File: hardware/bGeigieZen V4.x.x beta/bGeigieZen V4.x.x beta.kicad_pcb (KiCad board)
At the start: 2 copper layers, 129.4 x 64.6 mm, 12 parts, among them J1 M5 2x15 pin, J2 Geiger IRover, J3 GPS, J4 Geiger Safepulse, J5 Extra support header, J6 Grove

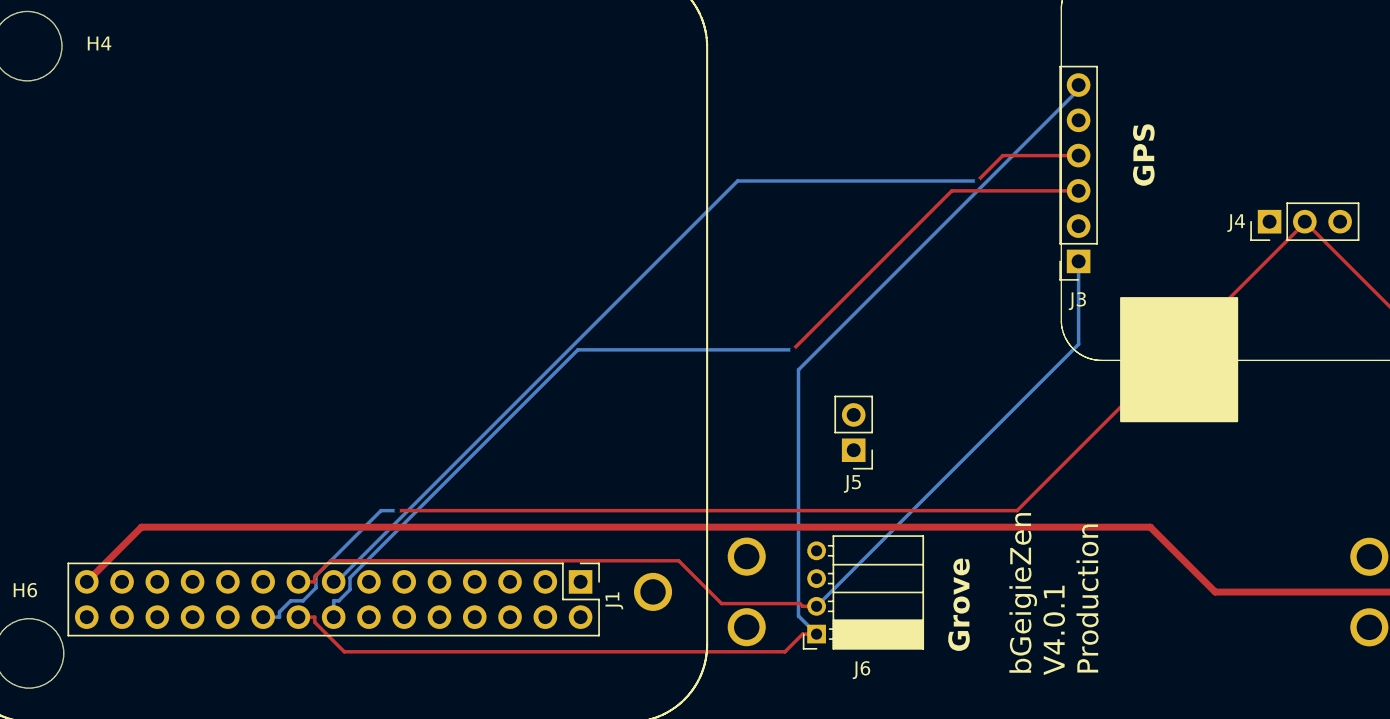
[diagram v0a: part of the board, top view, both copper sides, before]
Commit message: Small changes in copyright year and screen saver text
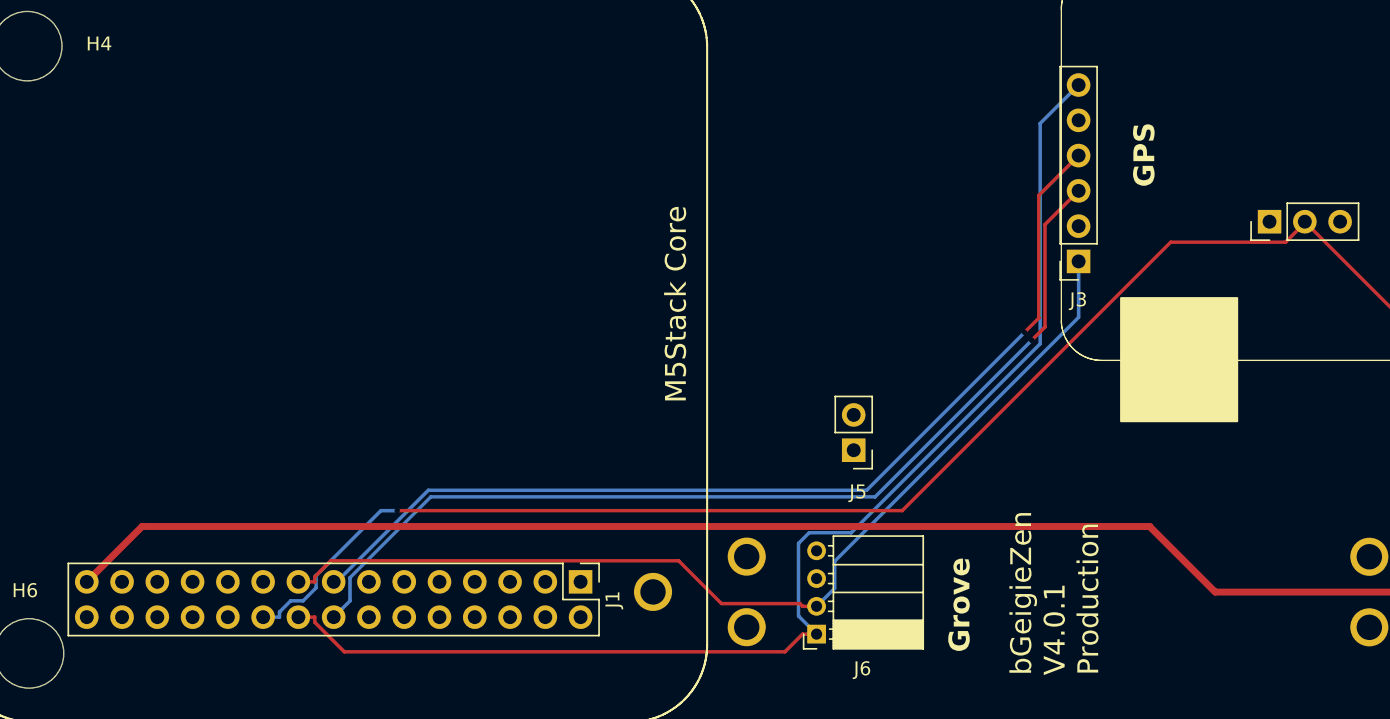
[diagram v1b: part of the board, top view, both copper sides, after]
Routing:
- net /RX2: track 66.4 -> 71.5 mm
- net /TX2: track 67.5 -> 71.7 mm
- net /SCL: track 87.5 -> 89.3 mm
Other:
- board text added: "M5Stack Core"
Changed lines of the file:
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@@
 (kicad_pcb
-	(version 20240108)
+	(version 20240225)
 	(generator "pcbnew")
 	(generator_version "8.99")
@@
 		(tags "Through hole pin header THT 1x02 2.54mm single row")
 		(property "Reference" "J5"
-			(at 0 -2.33 0)
+			(at -0.3208 -3.005 0)
 			(unlocked yes)
 			(layer "F.SilkS")
@@
 		(tags "Through hole pin header THT 1x03 2.54mm single row")
 		(property "Reference" "J4"
-			(at 0 -2.33 0)
+			(at 0.098 -3.4632 0)
 			(unlocked yes)
-			(layer "F.SilkS")
+			(layer "B.SilkS")
 			(effects
 				(font
@@
 					(thickness 0.15)
 				)
+				(justify mirror)
 			)
 		)
@@
 		)
 	)
+	(gr_text "M5Stack Core"
+		(at 148.336 96.4172 90)
+		(layer "F.SilkS")
+		(effects
+			(font
+				(size 1.5 1.5)
+				(thickness 0.3)
+			)
+		)
+	)
 	(gr_text "screws for the display are M3 12mm"
 		(at 106.7816 141.426 0)
@@
 	)
 	(segment
-		(start 177.317 85.7097)
-		(end 171.863 85.7097)
+		(start 174.4472 97.4154)
+		(end 174.4472 88.5795)
 		(width 0.25)
 		(layer "F.Cu")
@@
 	)
 	(segment
-		(start 171.863 85.7097)
-		(end 170.0347 87.538)
+		(start 173.4223 98.4403)
+		(end 174.4472 97.4154)
+		(width 0.25)
+		(layer "F.Cu")
+		(net 2)
+	)
+	(segment
+		(start 174.4472 88.5795)
+		(end 177.317 85.7097)
 		(width 0.25)
 		(layer "F.Cu")
@@
 	)
 	(via
-		(at 170.0347 87.538)
+		(at 173.4223 98.4403)
 		(size 0.3)
 		(drill 0.4)
@@
 	)
 	(segment
-		(start 123.8941 116.407)
-		(end 123.6726 116.407)
+		(start 162.052 109.8106)
+		(end 130.4905 109.8106)
 		(width 0.25)
 		(layer "B.Cu")
@@
 	)
 	(segment
-		(start 170.0347 87.538)
-		(end 152.7631 87.538)
+		(start 173.4223 98.4403)
+		(end 162.052 109.8106)
 		(width 0.25)
 		(layer "B.Cu")
@@
 	)
 	(segment
-		(start 152.7631 87.538)
+		(start 123.8941 116.407)
+		(end 123.6726 116.407)
+		(width 0.25)
+		(layer "B.Cu")
+		(net 2)
+	)
+	(segment
+		(start 130.4905 109.8106)
 		(end 123.8941 116.407)
 		(width 0.25)
@@
 	)
 	(segment
-		(start 177.317 88.2497)
-		(end 168.1844 88.2497)
+		(start 174.8972 98.05)
+		(end 174.8972 90.6695)
 		(width 0.25)
 		(layer "F.Cu")
@@
 	)
 	(segment
-		(start 168.1844 88.2497)
-		(end 156.739 99.6951)
+		(start 173.9392 99.008)
+		(end 174.8972 98.05)
+		(width 0.25)
+		(layer "F.Cu")
+		(net 3)
+	)
+	(segment
+		(start 174.8972 90.6695)
+		(end 177.317 88.2497)
 		(width 0.25)
 		(layer "F.Cu")
@@
 	)
 	(via
-		(at 156.739 99.6951)
+		(at 173.9392 99.008)
 		(size 0.3)
 		(drill 0.4)
@@
 	)
 	(segment
-		(start 123.6726 118.947)
-		(end 123.6726 117.7703)
+		(start 162.6616 110.2856)
+		(end 130.6698 110.2856)
 		(width 0.25)
 		(layer "B.Cu")
@@
 	)
 	(segment
-		(start 141.2603 99.6951)
-		(end 124.8493 116.1061)
+		(start 124.8493 116.1061)
+		(end 124.8493 117.7703)
 		(width 0.25)
 		(layer "B.Cu")
@@
 	)
 	(segment
-		(start 124.8493 116.9614)
-		(end 124.0404 117.7703)
+		(start 173.9392 99.008)
+		(end 162.6616 110.2856)
 		(width 0.25)
 		(layer "B.Cu")
@@
 	)
 	(segment
-		(start 124.8493 116.1061)
-		(end 124.8493 116.9614)
+		(start 124.8493 117.7703)
+		(end 123.6726 118.947)
 		(width 0.25)
 		(layer "B.Cu")
@@
 	)
 	(segment
-		(start 124.0404 117.7703)
-		(end 123.6726 117.7703)
+		(start 130.6698 110.2856)
+		(end 124.8493 116.1061)
 		(width 0.25)
 		(layer "B.Cu")
@@
 	)
 	(segment
-		(start 156.739 99.6951)
-		(end 141.2603 99.6951)
+		(start 193.6514 90.5138)
+		(end 192.2202 91.945)
 		(width 0.25)
-		(layer "B.Cu")
-		(net 3)
+		(layer "F.Cu")
+		(net 17)
+	)
+	(segment
+		(start 183.9486 91.945)
+		(end 164.6149 111.2787)
+		(width 0.25)
+		(layer "F.Cu")
+		(net 17)
 	)
 	(segment
-		(start 172.8865 111.2787)
+		(start 164.6149 111.2787)
 		(end 128.2448 111.2787)
 		(width 0.25)
@@
 	)
 	(segment
-		(start 193.6514 90.5138)
-		(end 172.8865 111.2787)
+		(start 192.2202 91.945)
+		(end 183.9486 91.945)
 		(width 0.25)
 		(layer "F.Cu")
@@
 	)
 	(segment
-		(start 177.317 99.2996)
+		(start 158.4476 118.169)
+		(end 159.7476 116.869)
+		(width 0.25)
+		(layer "B.Cu")
+		(net 23)
+	)
+	(segment
+		(start 177.317 97.3574)
 		(end 177.317 93.3297)
 		(width 0.25)
@@
 	)
 	(segment
-		(start 158.4476 118.169)
-		(end 177.317 99.2996)
+		(start 159.7476 114.9268)
+		(end 177.317 97.3574)
+		(width 0.25)
+		(layer "B.Cu")
+		(net 23)
+	)
+	(segment
+		(start 159.7476 116.869)
+		(end 159.7476 114.9268)
 		(width 0.25)
 		(layer "B.Cu")
@@
 	)
 	(segment
-		(start 157.1459 101.1418)
-		(end 177.317 80.9707)
+		(start 174.5488 83.3979)
+		(end 177.317 80.6297)
+		(width 0.25)
+		(layer "B.Cu")
+		(net 24)
+	)
+	(segment
+		(start 157.1476 118.869)
+		(end 157.1476 113.630522)
+		(width 0.25)
+		(layer "B.Cu")
+		(net 24)
+	)
+	(segment
+		(start 157.909122 112.869)
+		(end 160.9418 112.869)
+		(width 0.25)
+		(layer "B.Cu")
+		(net 24)
+	)
+	(segment
+		(start 157.1476 113.630522)
+		(end 157.909122 112.869)
 		(width 0.25)
 		(layer "B.Cu")
@@
 	(segment
 		(start 158.4476 120.169)
-		(end 157.1459 118.8673)
+		(end 157.1476 118.869)
 		(width 0.25)
 		(layer "B.Cu")
@@
 	)
 	(segment
-		(start 177.317 80.9707)
-		(end 177.317 80.6297)
+		(start 174.5488 99.262)
+		(end 174.5488 83.3979)
 		(width 0.25)
 		(layer "B.Cu")
@@
 	)
 	(segment
-		(start 157.1459 118.8673)
-		(end 157.1459 101.1418)
+		(start 160.9418 112.869)
+		(end 174.5488 99.262)
 		(width 0.25)
 		(layer "B.Cu")
@@
 	)
 	(segment
-		(start 109.8329 112.4667)
-		(end 105.8926 116.407)
+		(start 205.2376 117.14)
+		(end 187.1557 117.14)
 		(width 0.5)
 		(layer "F.Cu")
@@
 	)
 	(segment
-		(start 208.4126 117.14)
-		(end 205.2376 117.14)
+		(start 187.1557 117.14)
+		(end 182.4349 112.4192)
 		(width 0.5)
 		(layer "F.Cu")
@@
 	)
 	(segment
-		(start 205.2376 117.14)
-		(end 187.1557 117.14)
+		(start 208.4126 117.14)
+		(end 205.2376 117.14)
 		(width 0.5)
 		(layer "F.Cu")
@@
 	)
 	(segment
-		(start 187.1557 117.14)
-		(end 182.4824 112.4667)
+		(start 109.8804 112.4192)
+		(end 105.8926 116.407)
 		(width 0.5)
 		(layer "F.Cu")
@@
 	)
 	(segment
-		(start 182.4824 112.4667)
-		(end 109.8329 112.4667)
+		(start 182.4349 112.4192)
+		(end 109.8804 112.4192)
 		(width 0.5)
 		(layer "F.Cu")
